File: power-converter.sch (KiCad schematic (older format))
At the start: 16 parts, among them U2 TC1262-33VDB

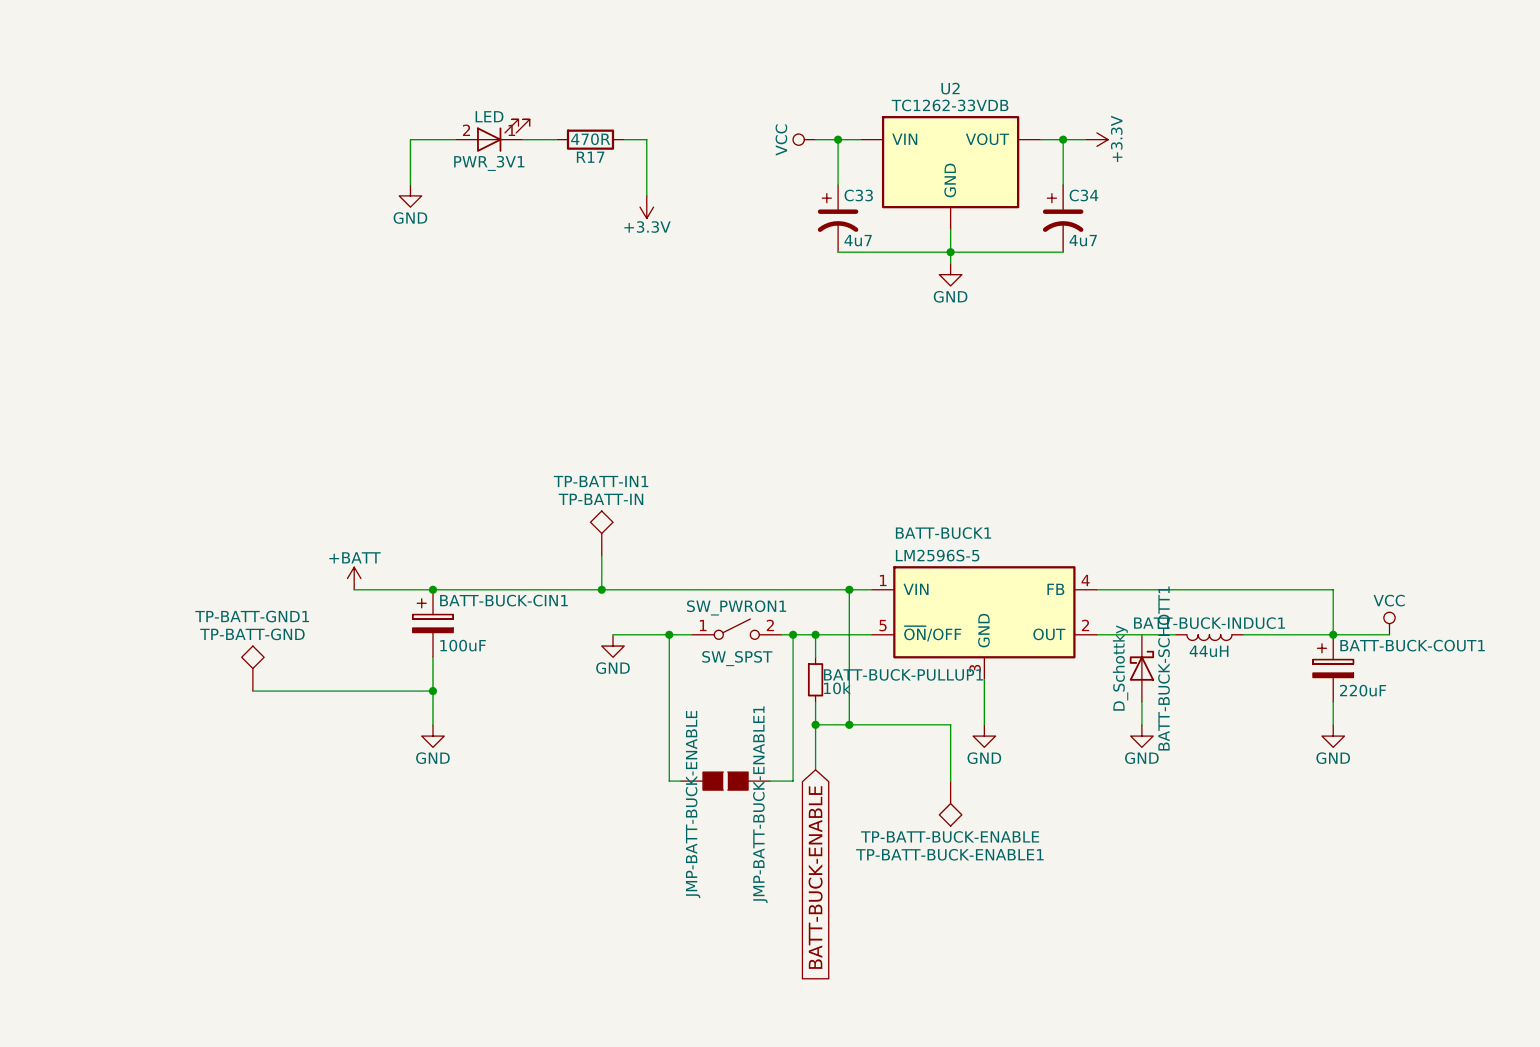
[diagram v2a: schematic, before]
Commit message: zone movement + routing of all circuits
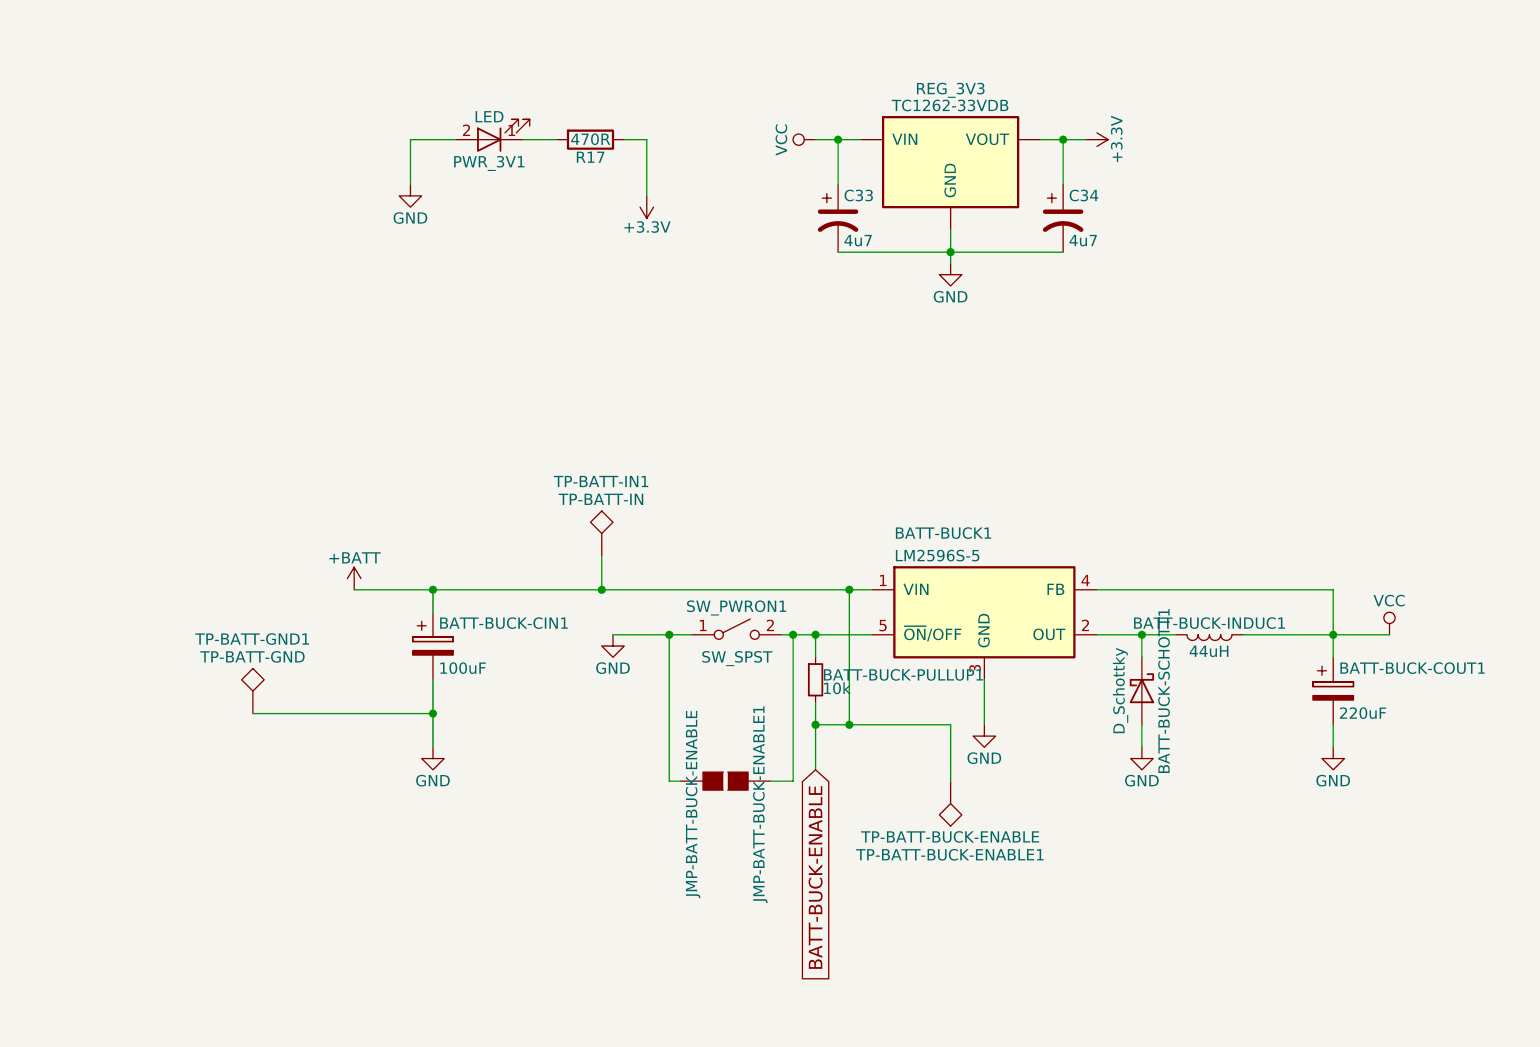
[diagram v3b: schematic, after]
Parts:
- BATT-BUCK-CIN1, BATT-BUCK-COUT1: footprint (none) -> Capacitors_SMD:CP_Elec_10x10.5
- BATT-BUCK-INDUC1: footprint (none) -> DR74-330-R:INDM7676X435N
- BATT-BUCK-PULLUP1: footprint (none) -> Resistors_SMD:R_0603
- BATT-BUCK-SCHOTT1: footprint (none) -> digikey-footprints:DO-214AB
- BATT-BUCK1: footprint TO_SOT_Packages_SMD:TO-263-5Lead -> TO_SOT_Packages_SMD:TO-263-5_TabPin3
- C33, C34: footprint (none) -> Capacitors_SMD:C_0603
- JMP-BATT-BUCK-ENABLE1: footprint Connectors:GS2 -> Connect:GS2
- TP-BATT-BUCK-ENABLE1, TP-BATT-GND1, TP-BATT-IN1: footprint (none) -> Measurement_Points:Measurement_Point_Round-SMD-Pad_Small
- renumbered U2 to REG_3V3
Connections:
- net at BATT-BUCK-INDUC1.2, BATT-BUCK1.2 (OUT): now also BATT-BUCK-SCHOTT1.K
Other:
- moved on the sheet: BATT-BUCK-CIN1, BATT-BUCK-COUT1, TP-BATT-GND1
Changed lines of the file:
@@
 EESchema Schematic File Version 2
 LIBS:power
-LIBS:device
 LIBS:transistors
 LIBS:conn
@@
 LIBS:sensors
 LIBS:dc-dc
+LIBS:device
 LIBS:dc26-cache
 EELAYER 25 0
@@
 $Descr A4 11693 8268
 encoding utf-8
-Sheet 3 6
+Sheet 2 6
 Title "Power Converter"
 Date ""
@@
 F 0 "BATT-BUCK1" H 6250 4150 50  0000 L CNN
 F 1 "LM2596S-5" H 6250 4050 50  0000 L CNN
-F 2 "TO_SOT_Packages_SMD:TO-263-5Lead" H 6950 3550 50  0001 C CIN
+F 2 "TO_SOT_Packages_SMD:TO-263-5_TabPin3" H 6950 3550 50  0001 C CIN
 F 3 "" H 6650 3800 50  0001 C CNN
 	1    6650 3800
@@
 	5750 3900 6150 3900
 $Comp
-L GND #PWR1232
+L GND #PWR025
 U 1 1 5B2D2C35
 P 5000 3900
-F 0 "#PWR1232" H 5000 3650 50  0001 C CNN
+F 0 "#PWR025" H 5000 3650 50  0001 C CNN
 F 1 "GND" H 5000 3750 50  0000 C CNN
 F 2 "" H 5000 3900 50  0001 C CNN
@@
 F 0 "BATT-BUCK-INDUC1" V 7600 3900 50  0000 C CNN
 F 1 "44uH" V 7725 3900 50  0000 C CNN
-F 2 "" H 7650 3900 50  0001 C CNN
+F 2 "DR74-330-R:INDM7676X435N" H 7650 3900 50  0001 C CNN
 F 3 "" H 7650 3900 50  0001 C CNN
 	1    7650 3900
@@
 	7150 3900 7500 3900
 $Comp
-L VCC #PWR1240
+L VCC #PWR026
 U 1 1 5B2D2C44
 P 8450 3900
-F 0 "#PWR1240" H 8450 3750 50  0001 C CNN
+F 0 "#PWR026" H 8450 3750 50  0001 C CNN
 F 1 "VCC" H 8450 4050 50  0000 C CNN
 F 2 "" H 8450 3900 50  0001 C CNN
@@
 	7150 3700 8200 3700
 Wire Wire Line
-	8200 3700 8200 3900
+	8200 3700 8200 4000
 Connection ~ 8200 3900
 $Comp
-L D_Schottky BATT-BUCK-SCHOTT1
-U 1 1 5B2D2C4E
-P 7350 4050
-F 0 "BATT-BUCK-SCHOTT1" H 7350 4150 50  0000 C CNN
-F 1 "D_Schottky" H 7350 3950 50  0000 C CNN
-F 2 "" H 7350 4050 50  0001 C CNN
-F 3 "" H 7350 4050 50  0001 C CNN
-	1    7350 4050
-	0    1    1    0
-$EndComp
-$Comp
-L GND #PWR1238
+L GND #PWR027
 U 1 1 5B2D2C55
-P 7350 4300
-F 0 "#PWR1238" H 7350 4050 50  0001 C CNN
-F 1 "GND" H 7350 4150 50  0000 C CNN
-F 2 "" H 7350 4300 50  0001 C CNN
-F 3 "" H 7350 4300 50  0001 C CNN
-	1    7350 4300
-	1    0    0    -1
-$EndComp
-Wire Wire Line
-	7350 4200 7350 4300
+P 7350 4400
+F 0 "#PWR027" H 7350 4150 50  0001 C CNN
+F 1 "GND" H 7350 4250 50  0000 C CNN
+F 2 "" H 7350 4400 50  0001 C CNN
+F 3 "" H 7350 4400 50  0001 C CNN
+	1    7350 4400
+	1    0    0    -1
+$EndComp
+Wire Wire Line
+	7350 4300 7350 4400
 $Comp
 L CP BATT-BUCK-COUT1
 U 1 1 5B2D2C5C
-P 8200 4050
-F 0 "BATT-BUCK-COUT1" H 8225 4150 50  0000 L CNN
-F 1 "220uF" H 8225 3950 50  0000 L CNN
-F 2 "" H 8238 3900 50  0001 C CNN
-F 3 "" H 8200 4050 50  0001 C CNN
-	1    8200 4050
-	1    0    0    -1
-$EndComp
-$Comp
-L GND #PWR1239
+P 8200 4150
+F 0 "BATT-BUCK-COUT1" H 8225 4250 50  0000 L CNN
+F 1 "220uF" H 8225 4050 50  0000 L CNN
+F 2 "Capacitors_SMD:CP_Elec_10x10.5" H 8238 4000 50  0001 C CNN
+F 3 "" H 8200 4150 50  0001 C CNN
+	1    8200 4150
+	1    0    0    -1
+$EndComp
+$Comp
+L GND #PWR028
 U 1 1 5B2D2C63
-P 8200 4300
-F 0 "#PWR1239" H 8200 4050 50  0001 C CNN
-F 1 "GND" H 8200 4150 50  0000 C CNN
-F 2 "" H 8200 4300 50  0001 C CNN
-F 3 "" H 8200 4300 50  0001 C CNN
-	1    8200 4300
-	1    0    0    -1
-$EndComp
-Wire Wire Line
-	8200 4200 8200 4300
-$Comp
-L GND #PWR1236
+P 8200 4400
+F 0 "#PWR028" H 8200 4150 50  0001 C CNN
+F 1 "GND" H 8200 4250 50  0000 C CNN
+F 2 "" H 8200 4400 50  0001 C CNN
+F 3 "" H 8200 4400 50  0001 C CNN
+	1    8200 4400
+	1    0    0    -1
+$EndComp
+Wire Wire Line
+	8200 4300 8200 4400
+$Comp
+L GND #PWR029
 U 1 1 5B2D2C6A
 P 6650 4300
-F 0 "#PWR1236" H 6650 4050 50  0001 C CNN
+F 0 "#PWR029" H 6650 4050 50  0001 C CNN
 F 1 "GND" H 6650 4150 50  0000 C CNN
 F 2 "" H 6650 4300 50  0001 C CNN
@@
 L CP BATT-BUCK-CIN1
 U 1 1 5B2D2C71
-P 4200 3850
-F 0 "BATT-BUCK-CIN1" H 4225 3950 50  0000 L CNN
-F 1 "100uF" H 4225 3750 50  0000 L CNN
-F 2 "" H 4238 3700 50  0001 C CNN
-F 3 "" H 4200 3850 50  0001 C CNN
-	1    4200 3850
+P 4200 3950
+F 0 "BATT-BUCK-CIN1" H 4225 4050 50  0000 L CNN
+F 1 "100uF" H 4225 3850 50  0000 L CNN
+F 2 "Capacitors_SMD:CP_Elec_10x10.5" H 4238 3800 50  0001 C CNN
+F 3 "" H 4200 3950 50  0001 C CNN
+	1    4200 3950
 	1    0    0    -1
 $EndComp
@@
 	3850 3700 6150 3700
 $Comp
-L GND #PWR1231
+L GND #PWR030
 U 1 1 5B2D2C79
-P 4200 4300
-F 0 "#PWR1231" H 4200 4050 50  0001 C CNN
-F 1 "GND" H 4200 4150 50  0000 C CNN
-F 2 "" H 4200 4300 50  0001 C CNN
-F 3 "" H 4200 4300 50  0001 C CNN
-	1    4200 4300
-	1    0    0    -1
-$EndComp
-Wire Wire Line
-	4200 4000 4200 4300
+P 4200 4400
+F 0 "#PWR030" H 4200 4150 50  0001 C CNN
+F 1 "GND" H 4200 4250 50  0000 C CNN
+F 2 "" H 4200 4400 50  0001 C CNN
+F 3 "" H 4200 4400 50  0001 C CNN
+	1    4200 4400
+	1    0    0    -1
+$EndComp
+Wire Wire Line
+	4200 4100 4200 4400
 $Comp
 L R_Small BATT-BUCK-PULLUP1
@@
 F 0 "BATT-BUCK-PULLUP1" H 5930 4120 50  0000 L CNN
 F 1 "10k" H 5930 4060 50  0000 L CNN
-F 2 "" H 5900 4100 50  0001 C CNN
+F 2 "Resistors_SMD:R_0603" H 5900 4100 50  0001 C CNN
 F 3 "" H 5900 4100 50  0001 C CNN
 	1    5900 4100
@@
 F 0 "JMP-BATT-BUCK-ENABLE1" H 5600 4700 50  0000 C CNN
 F 1 "JMP-BATT-BUCK-ENABLE" H 5600 4401 50  0000 C CNN
-F 2 "Connectors:GS2" V 5574 4550 50  0001 C CNN
+F 2 "Connect:GS2" V 5574 4550 50  0001 C CNN
 F 3 "" H 5500 4550 50  0001 C CNN
 	1    5500 4550
@@
 F 0 "TP-BATT-BUCK-ENABLE1" H 6500 4850 50  0000 C BNN
 F 1 "TP-BATT-BUCK-ENABLE" H 6500 4800 50  0000 C CNN
-F 2 "" H 6500 4550 50  0001 C CNN
+F 2 "Measurement_Points:Measurement_Point_Round-SMD-Pad_Small" H 6500 4550 50  0001 C CNN
 F 3 "" H 6500 4550 50  0001 C CNN
 	1    6500 4550
@@
 Connection ~ 6050 4300
 $Comp
-L +BATT #PWR1229
+L +BATT #PWR031
 U 1 1 5B2D2CA5
 P 3850 3700
-F 0 "#PWR1229" H 3850 3550 50  0001 C CNN
+F 0 "#PWR031" H 3850 3550 50  0001 C CNN
 F 1 "+BATT" H 3850 3840 50  0000 C CNN
 F 2 "" H 3850 3700 50  0001 C CNN
@@
 F 0 "TP-BATT-IN1" H 4950 3850 50  0000 C BNN
 F 1 "TP-BATT-IN" H 4950 3800 50  0000 C CNN
-F 2 "" H 4950 3550 50  0001 C CNN
+F 2 "Measurement_Points:Measurement_Point_Round-SMD-Pad_Small" H 4950 3550 50  0001 C CNN
 F 3 "" H 4950 3550 50  0001 C CNN
 	1    4950 3550
@@
 L TEST TP-BATT-GND1
 U 1 1 5B2D2CB5
-P 3400 4150
-F 0 "TP-BATT-GND1" H 3400 4450 50  0000 C BNN
-F 1 "TP-BATT-GND" H 3400 4400 50  0000 C CNN
-F 2 "" H 3400 4150 50  0001 C CNN
-F 3 "" H 3400 4150 50  0001 C CNN
-	1    3400 4150
-	1    0    0    -1
-$EndComp
-Wire Wire Line
-	3400 4150 4200 4150
-Connection ~ 4200 4150
-$Comp
-L +3.3V #PWR1233
+P 3400 4250
+F 0 "TP-BATT-GND1" H 3400 4550 50  0000 C BNN
+F 1 "TP-BATT-GND" H 3400 4500 50  0000 C CNN
+F 2 "Measurement_Points:Measurement_Point_Round-SMD-Pad_Small" H 3400 4250 50  0001 C CNN
+F 3 "" H 3400 4250 50  0001 C CNN
+	1    3400 4250
+	1    0    0    -1
+$EndComp
+Wire Wire Line
+	3400 4250 4200 4250
+Connection ~ 4200 4250
+$Comp
+L +3.3V #PWR032
 U 1 1 5B2DAE29
 P 5150 1950
-F 0 "#PWR1233" H 5150 1800 50  0001 C CNN
+F 0 "#PWR032" H 5150 1800 50  0001 C CNN
 F 1 "+3.3V" H 5150 2090 50  0000 C CNN
 F 2 "" H 5150 1950 50  0001 C CNN
@@
 $EndComp
 $Comp
-L TC1262-33VDB U2
+L TC1262-33VDB REG_3V3
 U 1 1 5B2DAE2F
 P 6500 1800
-F 0 "U2" H 6500 2125 50  0000 C CNN
+F 0 "REG_3V3" H 6500 2125 50  0000 C CNN
 F 1 "TC1262-33VDB" H 6500 2050 50  0000 C CNN
 F 2 "TO_SOT_Packages_SMD:SOT-223" H 6550 1550 50  0001 L CIN
@@
 $EndComp
 $Comp
-L +3.3V #PWR1237
+L +3.3V #PWR033
 U 1 1 5B2DAE36
 P 7100 1700
-F 0 "#PWR1237" H 7100 1550 50  0001 C CNN
+F 0 "#PWR033" H 7100 1550 50  0001 C CNN
 F 1 "+3.3V" H 7100 1840 50  0000 C CNN
 F 2 "" H 7100 1700 50  0001 C CNN
@@
 $EndComp
 $Comp
-L VCC #PWR1234
+L VCC #PWR034
 U 1 1 5B2DAE3C
 P 5900 1700
-F 0 "#PWR1234" H 5900 1550 50  0001 C CNN
+F 0 "#PWR034" H 5900 1550 50  0001 C CNN
 F 1 "VCC" H 5900 1850 50  0000 C CNN
 F 2 "" H 5900 1700 50  0001 C CNN
@@
 $EndComp
 $Comp
-L GND #PWR1235
+L GND #PWR035
 U 1 1 5B2DAE42
 P 6500 2250
-F 0 "#PWR1235" H 6500 2000 50  0001 C CNN
+F 0 "#PWR035" H 6500 2000 50  0001 C CNN
 F 1 "GND" H 6500 2100 50  0000 C CNN
 F 2 "" H 6500 2250 50  0001 C CNN
@@
 $EndComp
 $Comp
-L GND #PWR1230
+L GND #PWR036
 U 1 1 5B2DAE4F
 P 4100 1900
-F 0 "#PWR1230" H 4100 1650 50  0001 C CNN
+F 0 "#PWR036" H 4100 1650 50  0001 C CNN
 F 1 "GND" H 4100 1750 50  0000 C CNN
 F 2 "" H 4100 1900 50  0001 C CNN
@@
 F 0 "C33" H 6025 2150 50  0000 L CNN
 F 1 "4u7" H 6025 1950 50  0000 L CNN
-F 2 "" H 6000 2050 50  0001 C CNN
+F 2 "Capacitors_SMD:C_0603" H 6000 2050 50  0001 C CNN
 F 3 "" H 6000 2050 50  0001 C CNN
 	1    6000 2050
@@
 F 0 "C34" H 7025 2150 50  0000 L CNN
 F 1 "4u7" H 7025 1950 50  0000 L CNN
-F 2 "" H 7000 2050 50  0001 C CNN
+F 2 "Capacitors_SMD:C_0603" H 7000 2050 50  0001 C CNN
 F 3 "" H 7000 2050 50  0001 C CNN
 	1    7000 2050
@@
 	6000 1900 6000 1700
 Connection ~ 6000 1700
+Wire Wire Line
+	7350 4000 7350 3900
+Connection ~ 7350 3900
+Wire Wire Line
+	4200 3800 4200 3700
+$Comp
+L D_Schottky BATT-BUCK-SCHOTT1
+U 1 1 5B10C288
+P 7350 4150
+F 0 "BATT-BUCK-SCHOTT1" H 7350 4250 50  0000 C CNN
+F 1 "D_Schottky" H 7350 4050 50  0000 C CNN
+F 2 "digikey-footprints:DO-214AB" H 7350 4150 50  0001 C CNN
+F 3 "" H 7350 4150 50  0001 C CNN
+	1    7350 4150
+	0    1    1    0
+$EndComp
 $EndSCHEMATC
